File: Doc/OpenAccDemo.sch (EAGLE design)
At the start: 14 parts, among them IC1 PIC24FJ64GB002, IC2 XC6202P332TB

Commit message: change caption and copyright
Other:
- note added: "01/08/2011"
- note added: "Designed by magoroku15"
- note added: "OpenAccDemo V1.0"
- note removed: "05/28/2010"
- note removed: "Designed by Shunichi Yamamoto"
- note removed: "PICnome64 v1.1"
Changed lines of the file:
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@@
 <wire x1="134.112" y1="-57.658" x2="199.39" y2="-57.658" width="0.1524" layer="97"/>
 <wire x1="134.112" y1="-63.246" x2="199.39" y2="-63.246" width="0.1524" layer="97"/>
-<text x="152.4" y="-50.8" size="2.54" layer="97">PICnome64 v1.1</text>
-<text x="139.7" y="-55.88" size="2.54" layer="97">Designed by Shunichi Yamamoto</text>
-<text x="157.48" y="-62.23" size="2.54" layer="97">05/28/2010</text>
+<text x="152.4" y="-50.8" size="2.54" layer="97">OpenAccDemo V1.0</text>
+<text x="139.7" y="-55.88" size="2.54" layer="97">Designed by magoroku15</text>
+<text x="157.48" y="-62.23" size="2.54" layer="97">01/08/2011</text>
 <text x="134.62" y="-66.04" size="1.4224" layer="97">Released under Creative Commons Attribution-Share Alike 3.0 Unported</text>
 <frame x1="-66.04" y1="-71.12" x2="203.2" y2="127" columns="8" rows="5" layer="91"/>

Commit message: add a line VUSB to VDD.
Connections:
- net VCC: now also IC1.VUSB
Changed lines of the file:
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@@
 <part name="GND2" library="supply1" deviceset="GND" device=""/>
 <part name="P+1" library="supply1" deviceset="VCC" device=""/>
-<part name="P+2" library="supply1" deviceset="VCC" device="" value="VDD"/>
 <part name="R2" library="resistor" deviceset="R-US_" device="0204/5" value="10k"/>
 <part name="R3" library="resistor" deviceset="R-US_" device="0204/5" value="10k"/>
@@
 <part name="P+3" library="supply1" deviceset="VCC" device=""/>
 <part name="GND4" library="supply1" deviceset="GND" device=""/>
+<part name="P+4" library="supply1" deviceset="VCC" device="" value="VDD"/>
 </parts>
 <sheets>
@@
 <instance part="GND2" gate="1" x="149.86" y="73.66"/>
 <instance part="P+1" gate="VCC" x="149.86" y="106.68"/>
-<instance part="P+2" gate="VCC" x="99.06" y="60.96"/>
 <instance part="R2" gate="G$1" x="25.4" y="45.72" rot="R90"/>
 <instance part="R3" gate="G$1" x="12.7" y="45.72" rot="R90"/>
@@
 <instance part="P+3" gate="VCC" x="116.84" y="60.96"/>
 <instance part="GND4" gate="1" x="86.36" y="76.2"/>
+<instance part="P+4" gate="VCC" x="104.14" y="60.96"/>
 </instances>
 <busses>
@@
 </segment>
 <segment>
-<pinref part="IC1" gate="G$1" pin="VDD@2"/>
-<pinref part="P+2" gate="VCC" pin="VCC"/>
-<wire x1="99.06" y1="27.94" x2="99.06" y2="58.42" width="0.1524" layer="91"/>
-</segment>
-<segment>
 <pinref part="IC1" gate="G$1" pin="VBUS"/>
 <wire x1="99.06" y1="-5.08" x2="116.84" y2="-5.08" width="0.1524" layer="91"/>
@@
 <pinref part="P+3" gate="VCC" pin="VCC"/>
 </segment>
+<segment>
+<pinref part="P+4" gate="VCC" pin="VCC"/>
+<wire x1="104.14" y1="58.42" x2="104.14" y2="60.96" width="0.1524" layer="91"/>
+<pinref part="IC1" gate="G$1" pin="VUSB"/>
+<wire x1="99.06" y1="15.24" x2="104.14" y2="15.24" width="0.1524" layer="91"/>
+<wire x1="104.14" y1="15.24" x2="104.14" y2="27.94" width="0.1524" layer="91"/>
+<pinref part="IC1" gate="G$1" pin="VDD@2"/>
+<wire x1="104.14" y1="27.94" x2="104.14" y2="58.42" width="0.1524" layer="91"/>
+<wire x1="99.06" y1="27.94" x2="104.14" y2="27.94" width="0.1524" layer="91"/>
+<junction x="104.14" y="27.94"/>
+</segment>
 </net>

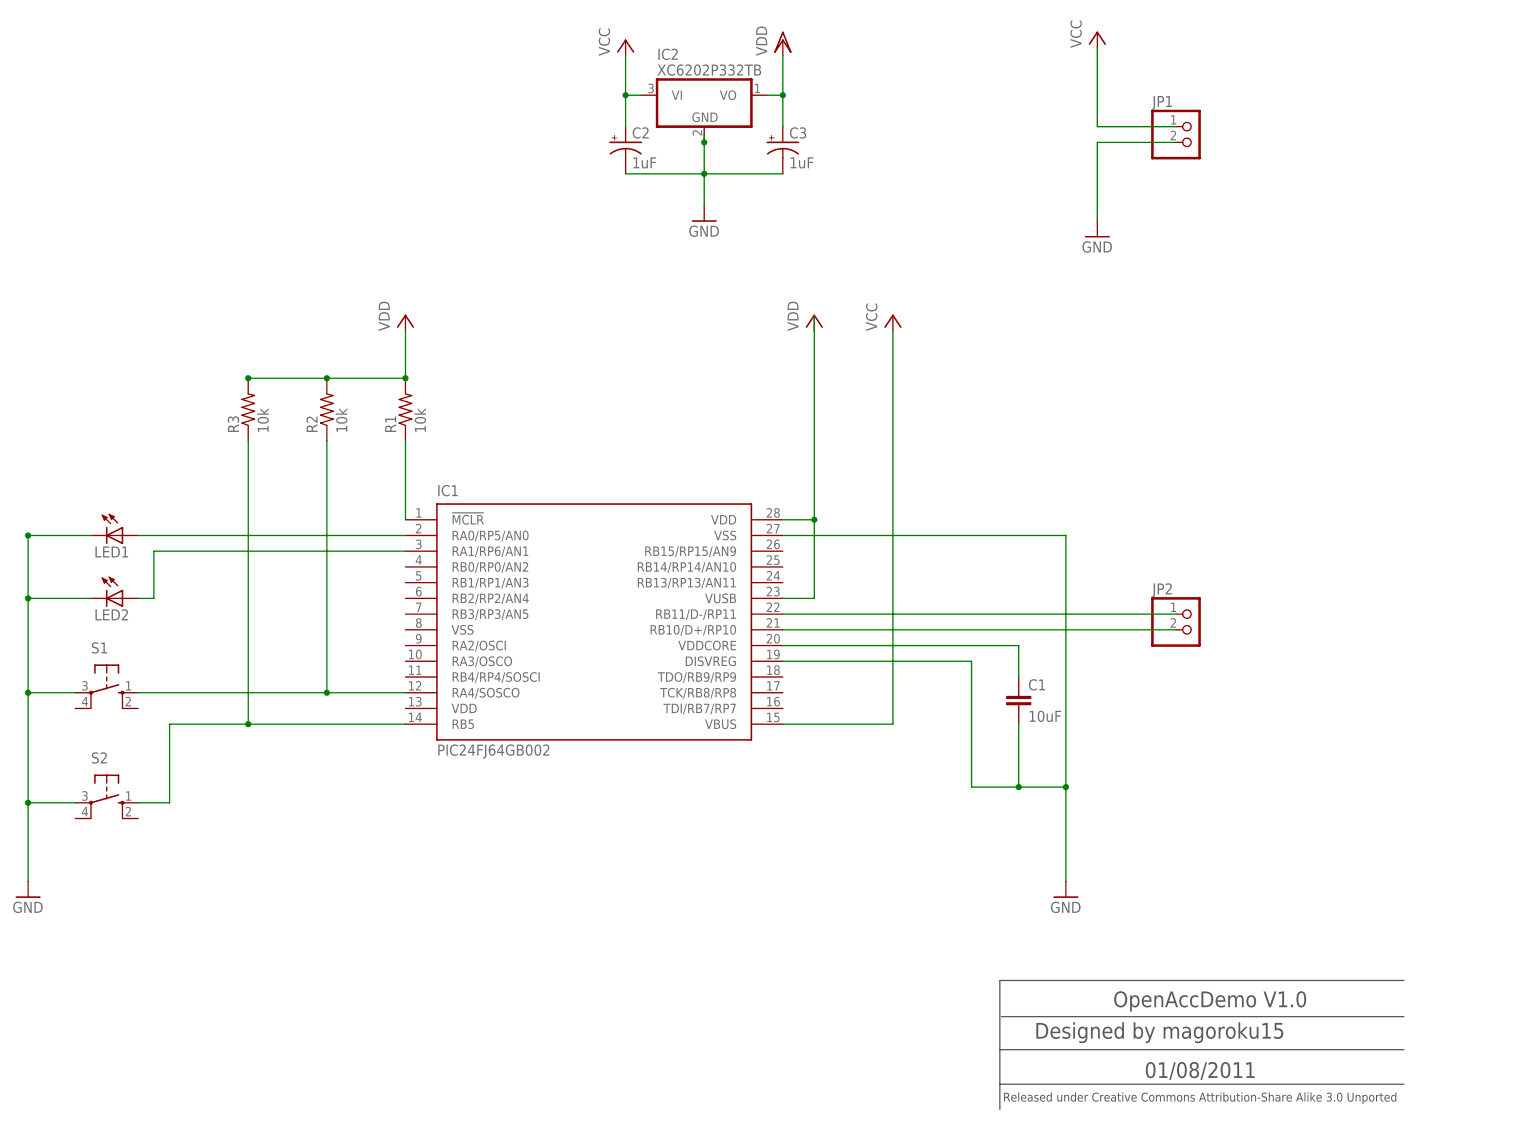
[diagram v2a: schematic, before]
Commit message: 可変抵抗の記述を追加
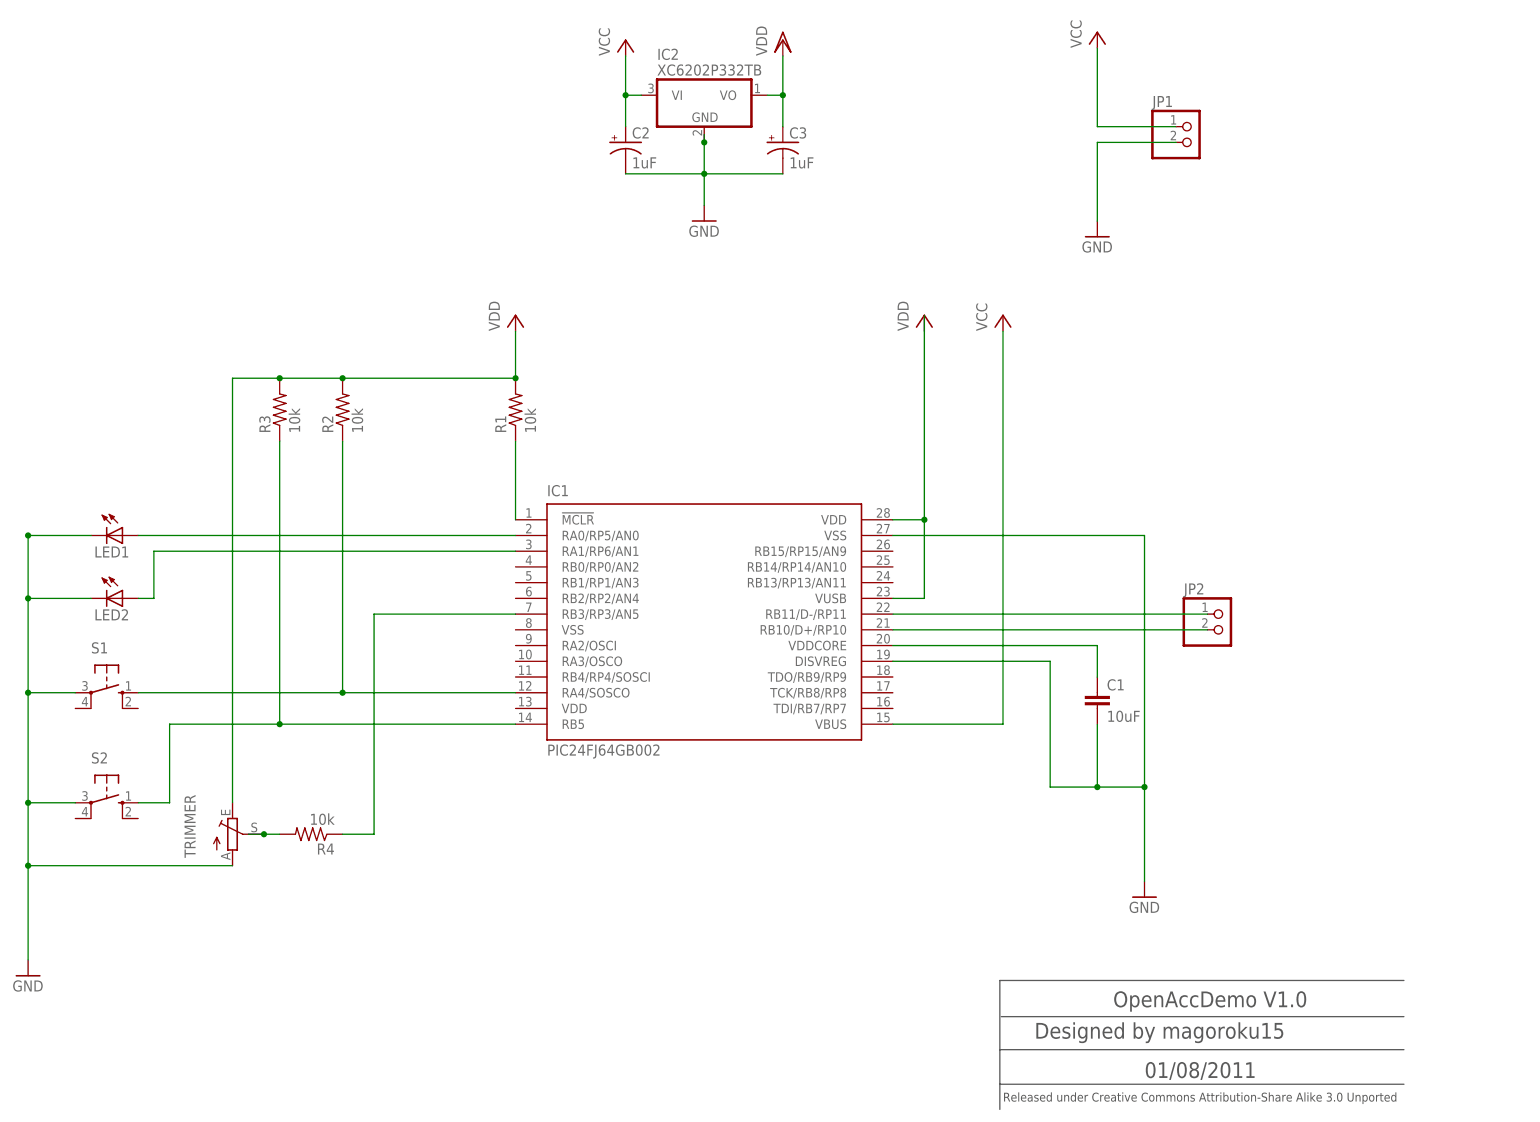
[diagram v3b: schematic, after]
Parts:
- added R4: 10k, resistor:R-US_0204/5
- added TRIMMER: (no value), pot:TRIM_EU-B25P
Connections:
- new net N$11: R4.2, TRIMMER.S
- new net N$6: IC1.RB3/RP3/AN5, R4.1
- net GND: now also TRIMMER.A
- net VCC: now also TRIMMER.E
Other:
- moved on the sheet: C1, IC1, JP2, R1, R2, R3
